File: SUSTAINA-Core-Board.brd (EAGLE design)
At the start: 120 x 70 mm, 67 parts, among them IC1 LTC4418IUF, M1 POWER-MONITOR-MODULE, M2 POWER-MONITOR-MODULE, M3 BUCK-BOOST-SWITCH-MODE-POWER-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, M4 POWER-MONITOR-MODULE, M5 POWER-MONITOR-MODULE, Q1 SUM110P06-08L-E3, Q2 SUM110P06-08L-E3, Q3 SUM110P06-08L-E3, Q4 SUM110P06-08L-E3, Q5 SUM110P06-08L-E3, Q6 SUM110P06-08L-E3

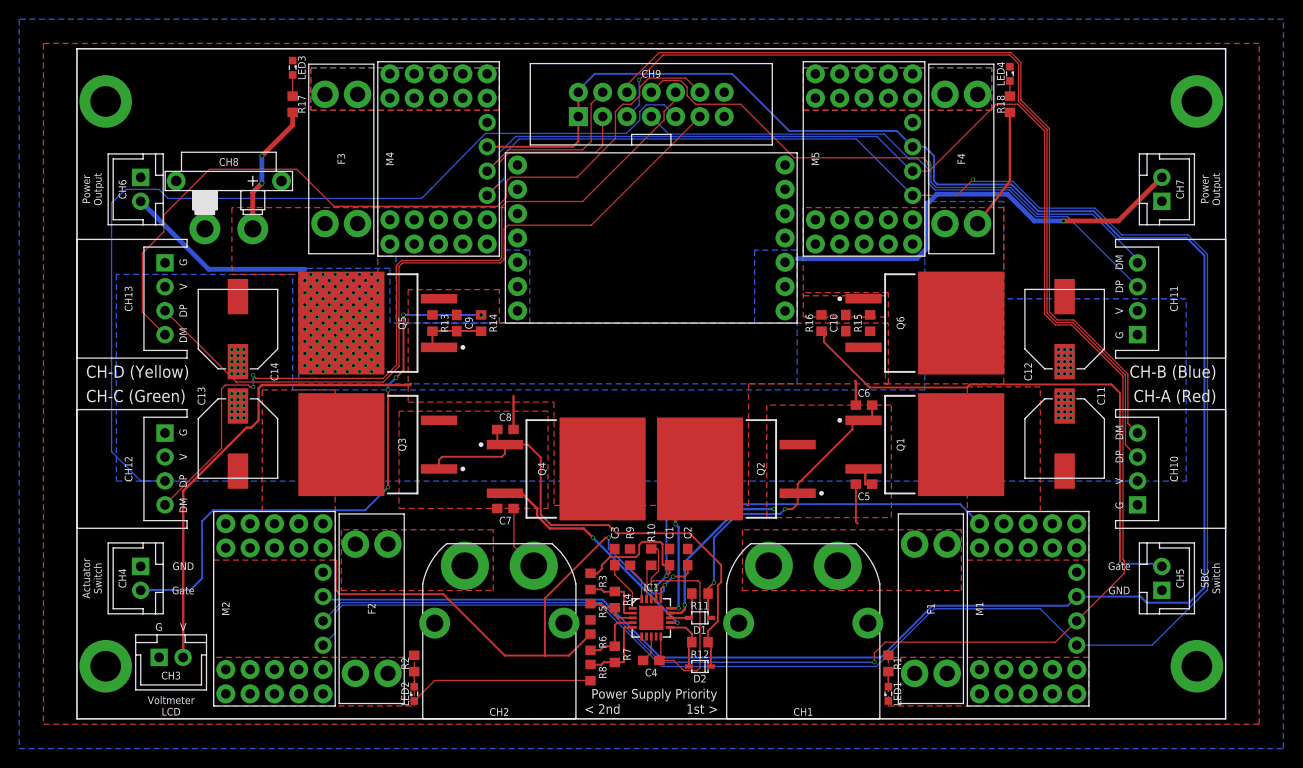
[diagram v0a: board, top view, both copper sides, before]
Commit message: Minimum net thickness changed from 5mil to 8mil
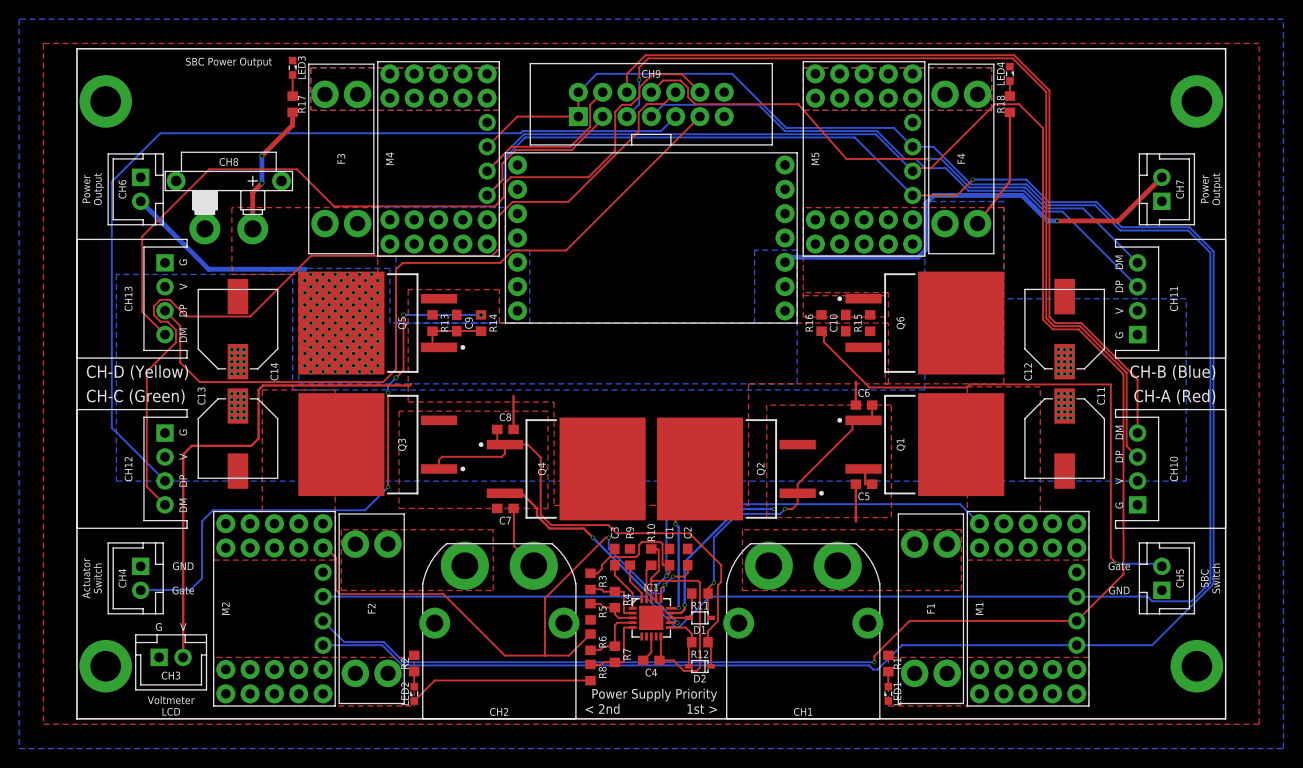
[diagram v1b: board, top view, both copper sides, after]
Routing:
- net I2C_SDA: track 243.6 -> 235.1 mm
- net C-DM: track 86.2 -> 92.6 mm, vias 2 -> 0
- net +3V3: track 223.5 -> 218.7 mm
- net G2: track 57.1 -> 54.0 mm
- net +POWER_INPUT: track 70.1 -> 73.2 mm
- net C-DP: track 98.0 -> 95.3 mm
- net I2C_SCL: track 225.5 -> 223.3 mm
- net +BATTERY_INPUT_SENSING2: track 63.8 -> 65.7 mm
- net +SBC_POWER_INPUT: track 67.4 -> 68.8 mm
- net G1: track 35.2 -> 33.8 mm
- net VS1: track 21.9 -> 20.8 mm
- net A-DM: track 88.5 -> 89.6 mm
- net B-DM: track 61.0 -> 60.0 mm
- net A-DP: track 92.7 -> 93.7 mm
- net D-DM: track 83.3 -> 84.2 mm
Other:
- board text added: "SBC Power Output"
